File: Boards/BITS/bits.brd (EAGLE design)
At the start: 71.4 x 86.6 mm, 38 parts, among them T1 SI1013, U1 LMR16020, X1 22-23-2021, X2 53398-10, X3 22-23-2031, X4 22-23-2041

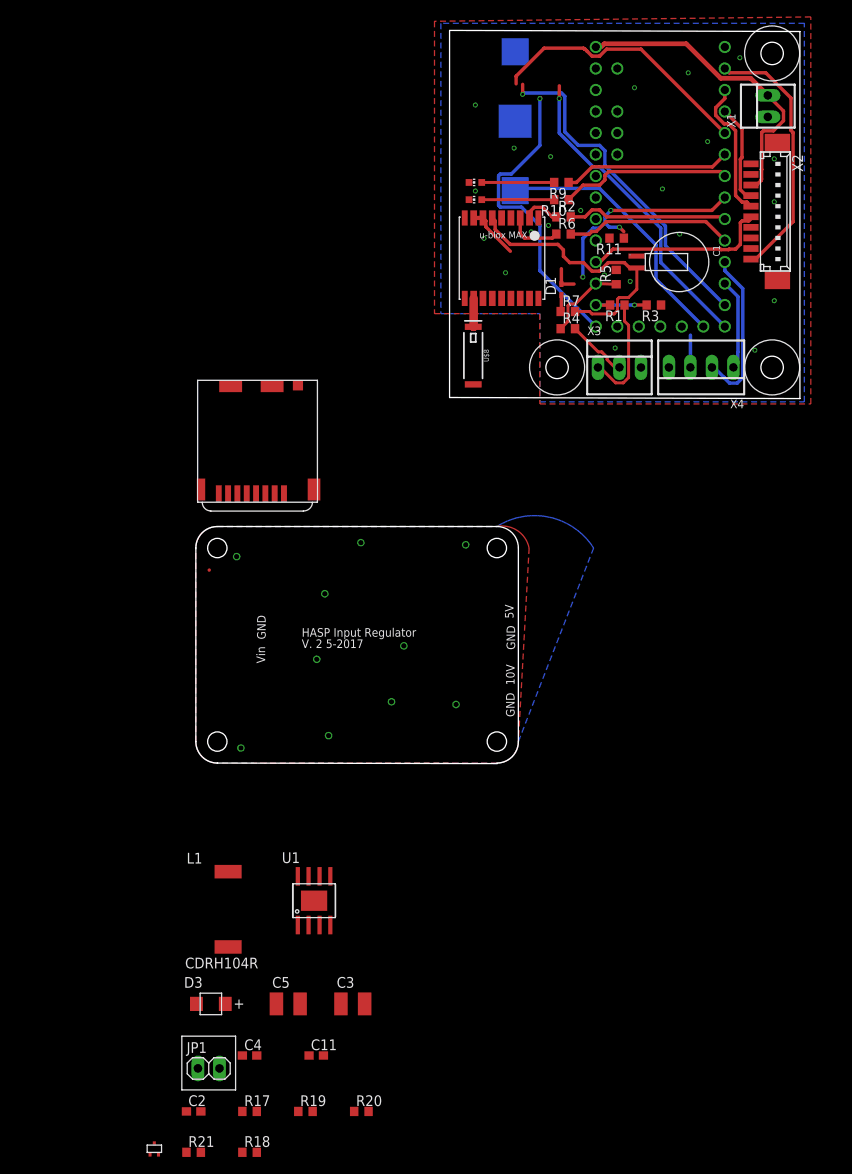
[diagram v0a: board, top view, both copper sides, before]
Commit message: General board parts placement for BITS
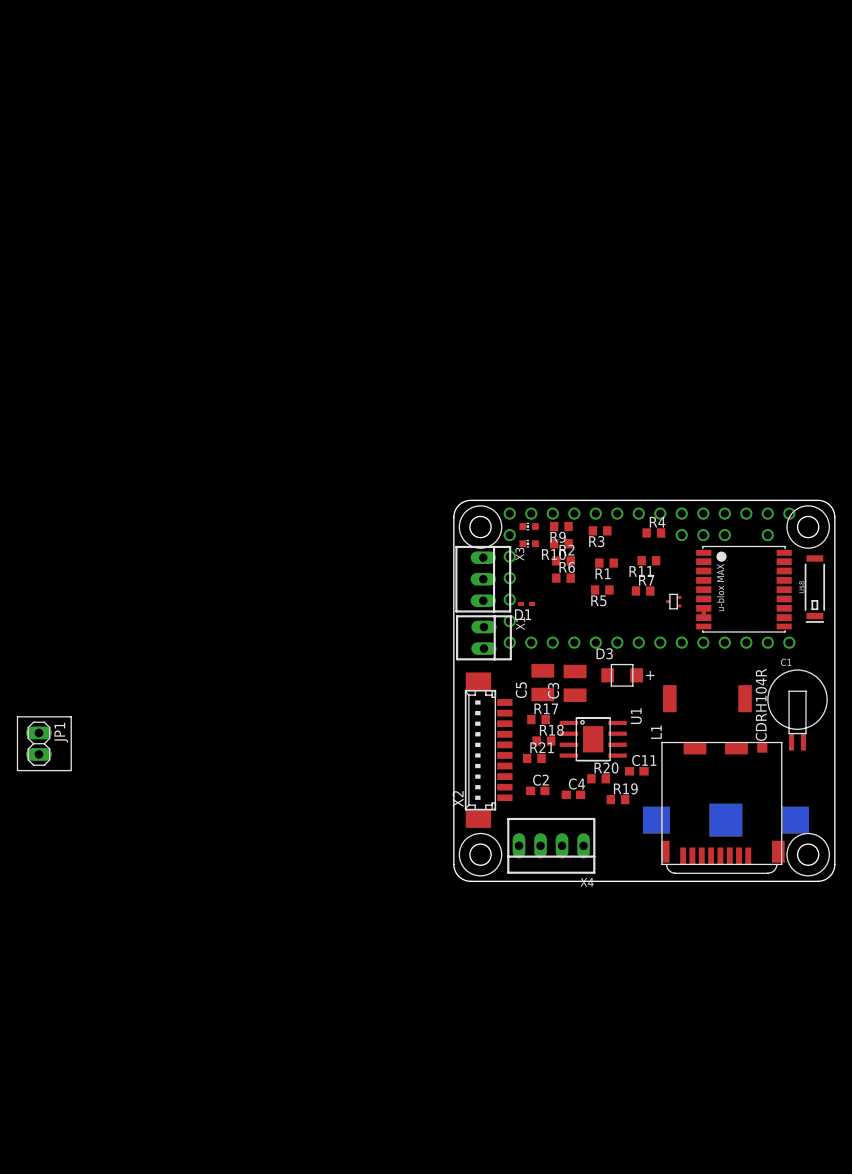
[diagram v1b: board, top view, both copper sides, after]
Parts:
- moved T1 90.4 mm to (26.9, 32.4), turned to 90 degrees
- moved U$3 86.2 mm to (32.1, 7.24), turned to 180 degrees
- moved X2 72.2 mm to (3.52, 15.5), turned to 90 degrees
- moved X1 71.2 mm to (3.56, 28.8), turned to 270 degrees
- moved U$4 69.6 mm to (34.8, 16.4)
- moved D3 62.2 mm to (19.9, 24.3)
- moved L1 61.8 mm to (30.0, 21.6), turned to 90 degrees
- moved R21 61.5 mm to (9.51, 14.5)
- moved R18 59.7 mm to (10.6, 16.6)
- moved X4 59.2 mm to (11.5, 4.19)
- moved C1 57.9 mm to (40.6, 18.0), turned to 0 degrees
- moved R17 57.5 mm to (10.0, 19.1)
- moved C2 55.5 mm to (9.91, 10.7)
- moved R19 52.1 mm to (19.4, 9.65)
- moved C11 50.6 mm to (21.6, 13.0)
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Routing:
- net MOSI: track 40.3 -> 0.00 mm, vias 1 -> 0
- net MISO: track 37.0 -> 0.00 mm, vias 1 -> 0
- net +5V: track 36.4 -> 0.00 mm
- net SCK: track 36.1 -> 0.00 mm, vias 1 -> 0
- net V_BCKP: track 33.4 -> 0.00 mm
- net VBAT: track 32.8 -> 0.00 mm
- net SD_CS: track 31.8 -> 0.00 mm
- net RXD: track 30.8 -> 0.00 mm
- net GPSON: track 26.6 -> 0.00 mm, vias 3 -> 0
- net RING: track 22.2 -> 0.00 mm
- net LED2: track 20.3 -> 0.00 mm
- net LED1: track 19.8 -> 0.00 mm
- net TX3: track 19.7 -> 0.00 mm
- net DOUT: track 19.2 -> 0.00 mm
- net RX3: track 19.0 -> 0.00 mm
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- removed copper zone on layer 1, net GND
- removed copper zone on layer 16, net GND
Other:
- board size 71.4 x 86.6 mm -> 45 x 45 mm
- board text removed: "10V"
- board text removed: "5V"
- board text removed: "GND"
- board text removed: "HASP Input Regulator"
- board text removed: "V. 2 5-2017"
- board text removed: "Vin"
